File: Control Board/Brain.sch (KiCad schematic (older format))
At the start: 36 parts, among them J10 USB_B_Micro, J11 Conn_ARM_JTAG_SWD_10, J9 Conn_ARM_JTAG_SWD_10, SW2 SW_Push, U1 ATSAMD21G, U6 AT24C32, Y1 32768Hz

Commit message: Soldered V2.0 pcb.
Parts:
- C1, C2: value 6.7pF -> 6.8pF
- C50: value 4.7uF -> 10uF
- U1: value ATSAMD21G -> ATSAMD21G18A-AU
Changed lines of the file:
@@
 P 9250 3000
 F 0 "U1" H 9250 4667 50  0000 C CNN
-F 1 "ATSAMD21G" H 9250 4576 50  0000 C CNN
+F 1 "ATSAMD21G18A-AU" H 9250 4576 50  0000 C CNN
 F 2 "Package_QFP:TQFP-48_7x7mm_P0.5mm" H 9250 2800 50  0001 L CNN
 F 3 "" H 9250 2800 50  0001 L CNN
@@
 AR Path="/60488463/6037167D" Ref="C2"  Part="1"
 F 0 "C2" H 7415 2946 50  0000 L CNN
-F 1 "6.7pF" H 7415 2855 50  0000 L CNN
+F 1 "6.8pF" H 7415 2855 50  0000 L CNN
 F 2 "Capacitor_SMD:C_0805_2012Metric_Pad1.18x1.45mm_HandSolder" H 7338 2750 50  0001 C CNN
 F 3 "~" H 7300 2900 50  0001 C CNN
@@
 AR Path="/60488463/60371DFA" Ref="C1"  Part="1"
 F 0 "C1" H 6686 2946 50  0000 R CNN
-F 1 "6.7pF" H 6686 2855 50  0000 R CNN
+F 1 "6.8pF" H 6686 2855 50  0000 R CNN
 F 2 "Capacitor_SMD:C_0805_2012Metric_Pad1.18x1.45mm_HandSolder" H 6838 2750 50  0001 C CNN
 F 3 "~" H 6800 2900 50  0001 C CNN
@@
 AR Path="/60488463/6048B387" Ref="C50"  Part="1"
 F 0 "C50" H 6200 2950 50  0000 L CNN
-F 1 "4.7uF" H 6200 2850 50  0000 L CNN
+F 1 "10uF" H 6200 2850 50  0000 L CNN
 F 2 "Capacitor_SMD:C_0805_2012Metric_Pad1.18x1.45mm_HandSolder" H 6238 2600 50  0001 C CNN
 F 3 "~" H 6200 2750 50  0001 C CNN

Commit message: Start of V2.1 PCB.
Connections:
- net ESP32_SCL: now also U1.14 (PA09/~~D3/SCL2); no longer U1.23 (PA14/~~D4)
- net ESP32_SDA: now also U1.23 (PA14/~~D4); no longer U1.14 (PA09/~~D3/SCL2)
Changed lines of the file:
@@
 Sheet 4 5
 Title "IoT12-hardware brain"
-Date "2021-02-22"
-Rev "V2.0"
+Date "2021-03-07"
+Rev "V2.1"
 Comp ""
 Comment1 ""
@@
 	0    -1   -1   0
 $EndComp
-Text GLabel 10500 2000 2    50   BiDi ~ 0
+Text GLabel 10500 2100 2    50   BiDi ~ 0
 ESP32_SDA
 Wire Wire Line
@@
 Text Notes 600  5500 0    118  ~ 0
 The pull is strong
-Text GLabel 10500 2100 2    50   Input ~ 0
+Text GLabel 10500 2000 2    50   Input ~ 0
 ESP32_SCL
 Wire Notes Line

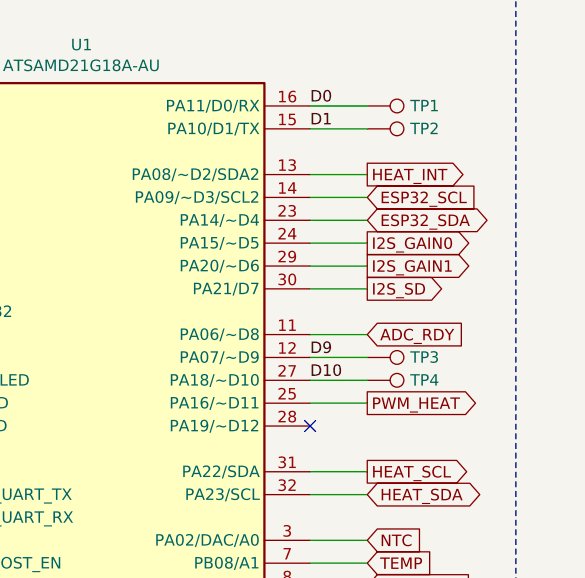
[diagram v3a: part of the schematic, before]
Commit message: Samd21 D2, D4 where swapped in symbol. No pcb change.
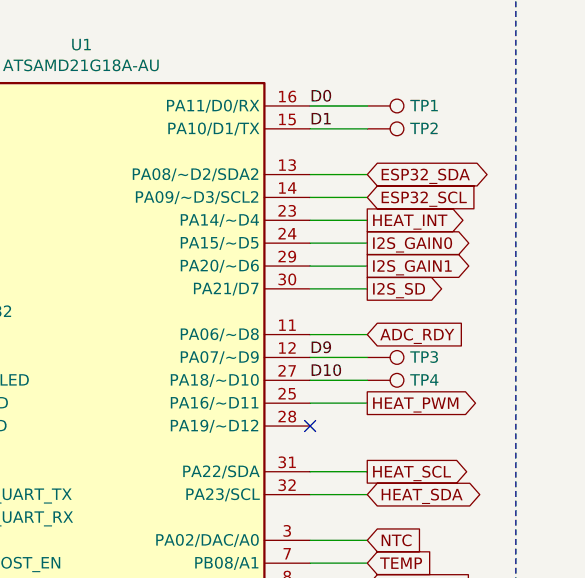
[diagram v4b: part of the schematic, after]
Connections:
- net ESP32_SDA: now also U1.13 (PA08/~~D2/SDA2); no longer U1.23 (PA14/~~D4)
- net HEAT_INT: now also U1.23 (PA14/~~D4); no longer U1.13 (PA08/~~D2/SDA2)
- net PWM_HEAT renamed HEAT_PWM
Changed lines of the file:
@@
 Sheet 4 5
 Title "IoT12-hardware brain"
-Date "2021-03-08"
+Date "2021-03-12"
 Rev "V2.1"
 Comp ""
@@
 Debug LED
 Text GLabel 10500 2900 2    50   Output ~ 0
-PWM_HEAT
+HEAT_PWM
 Wire Wire Line
 	10500 2900 10250 2900
@@
 Text GLabel 10500 3500 2    50   Input ~ 0
 NTC
-Text GLabel 10500 1900 2    50   Output ~ 0
+Text GLabel 10500 2100 2    50   Output ~ 0
 HEAT_INT
 Wire Wire Line
-	10250 1900 10500 1900
+	10250 2100 10500 2100
 Text GLabel 10500 2200 2    50   Output ~ 0
 I2S_GAIN0
@@
 	0    -1   -1   0
 $EndComp
-Text GLabel 10500 2100 2    50   BiDi ~ 0
+Text GLabel 10500 1900 2    50   BiDi ~ 0
 ESP32_SDA
 Wire Wire Line
@@
 	10500 3500 10250 3500
 Wire Wire Line
-	10500 2100 10250 2100
+	10500 1900 10250 1900
 NoConn ~ 8250 3600
 NoConn ~ 8250 3400

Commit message: More erratum.
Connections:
- net HEAT_SCL: now also U1.32 (PA23/SCL); no longer U1.31 (PA22/SDA)
- net HEAT_SDA: now also U1.31 (PA22/SDA); no longer U1.32 (PA23/SCL)
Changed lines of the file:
@@
 Sheet 4 5
 Title "IoT12-hardware brain"
-Date "2021-03-12"
+Date "2021-03-13"
 Rev "V2.1"
 Comp ""
@@
 	1    0    0    -1
 $EndComp
-Text GLabel 10500 3200 2    50   Output ~ 0
+Text GLabel 10500 3300 2    50   Output ~ 0
 HEAT_SCL
 Wire Wire Line
-	10500 3200 10250 3200
-Text GLabel 10500 3300 2    50   BiDi ~ 0
+	10500 3300 10250 3300
+Text GLabel 10500 3200 2    50   BiDi ~ 0
 HEAT_SDA
 $Comp
@@
 	11150 5200 11150 550
 Wire Wire Line
-	10500 3300 10250 3300
+	10500 3200 10250 3200
 Wire Wire Line
 	7850 1600 8250 1600
